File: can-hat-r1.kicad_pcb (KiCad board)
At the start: 2 copper layers, 65 x 55 mm, 61 parts, among them P1 PINBALL-CONNECTOR, P2 PINBALL-CONNECTOR, P3 PIHAT, Q1 DMG2305UX, Q2 DMMT5401, U1 MCP2562, U2 MCP2515, U3 AP3513E, U4 CAT24C32, X1 CRYSTAL

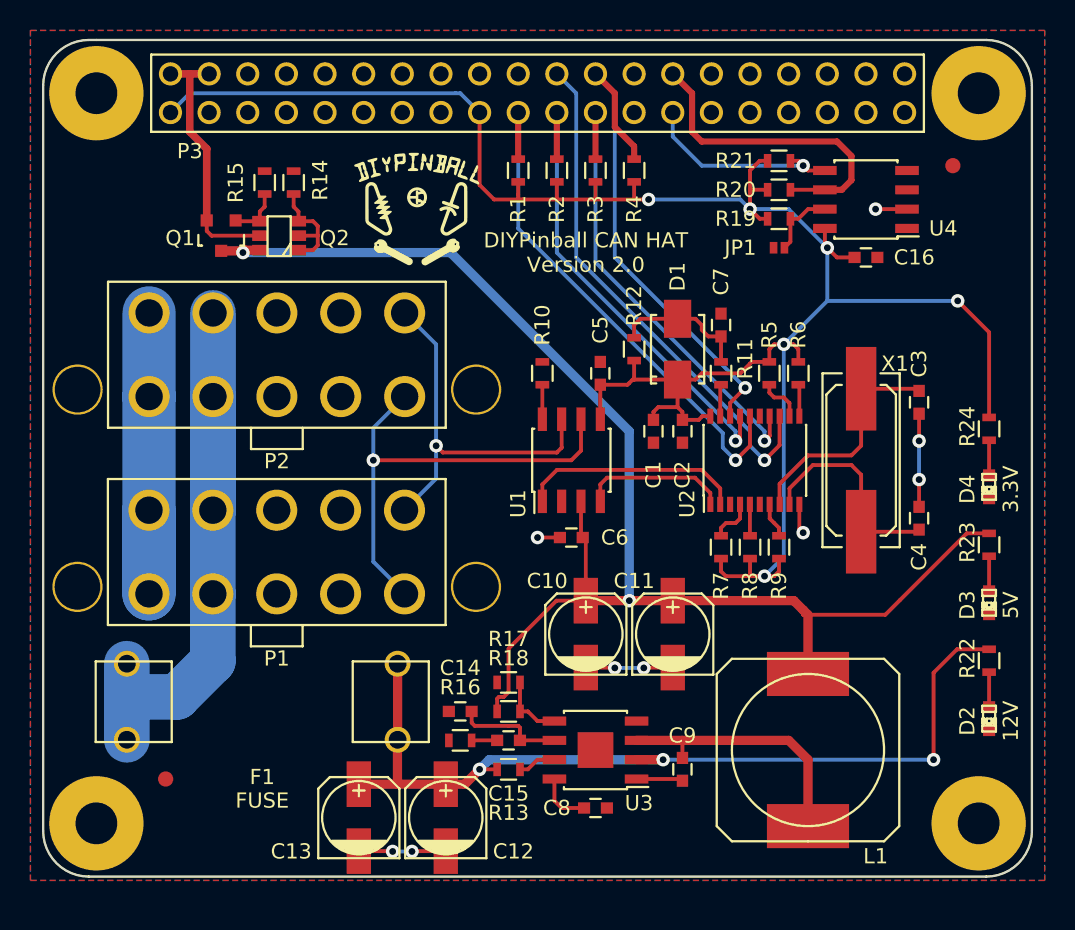
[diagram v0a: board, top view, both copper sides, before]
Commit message: Updating to correct wrong board dimensions (was 1mm too short) and to fix copper around screw holes (there shouldn't be any).
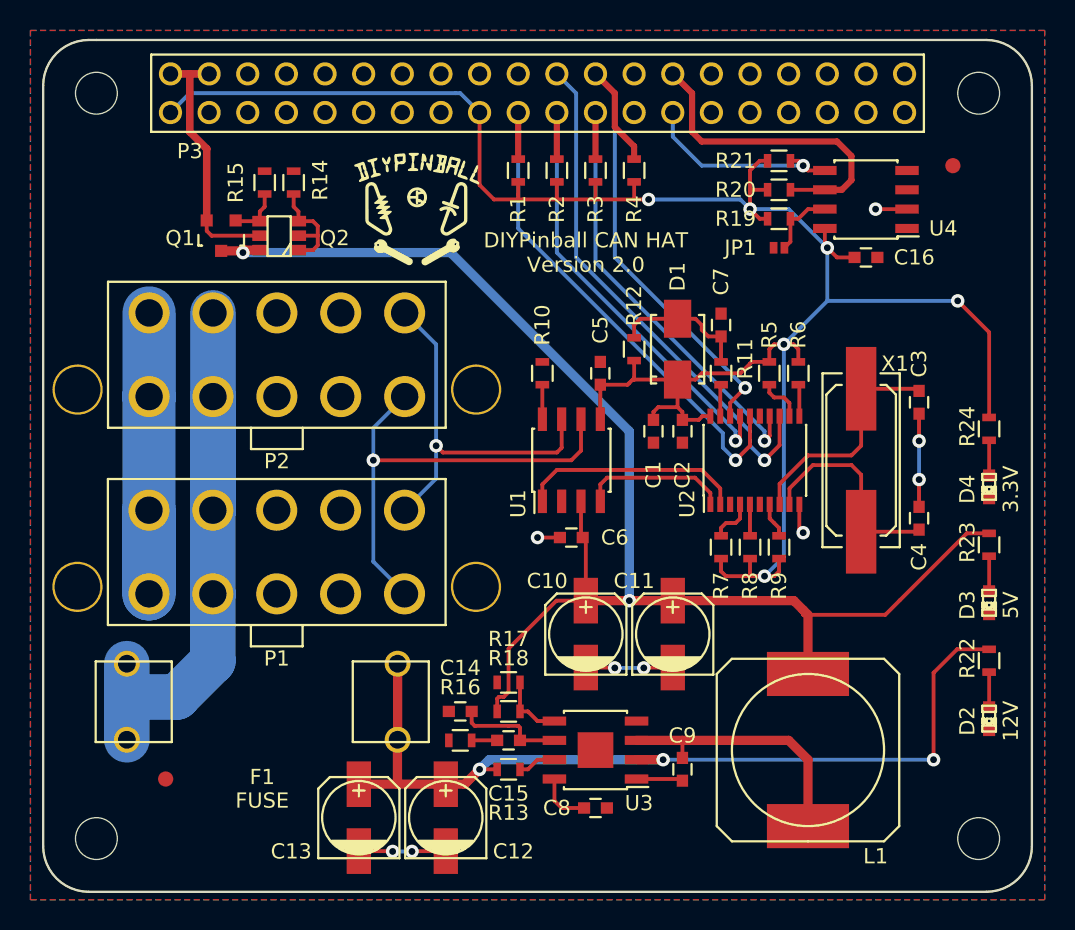
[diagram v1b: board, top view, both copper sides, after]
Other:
- board size 65 x 55 mm -> 65 x 56 mm

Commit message: Updated to latest version of KiCAD. Added PDF of schematic.
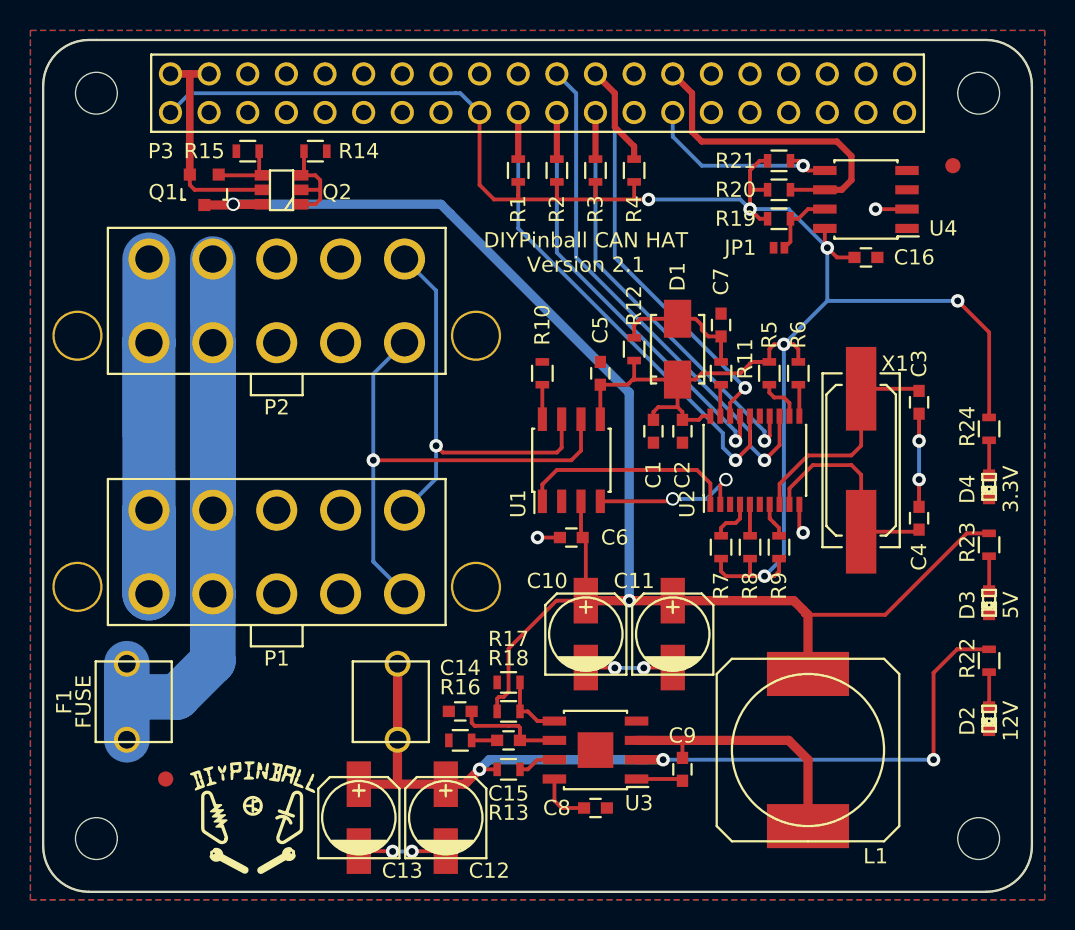
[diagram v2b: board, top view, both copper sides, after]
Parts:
- moved G*** 41.4 mm to (192.7, 150.2)
- moved P2 3.54 mm to (194.3, 116.2)
- moved Q1 3.21 mm to (189.5, 108.9)
- moved Q2 3.02 mm to (194.6, 108.9)
- moved R14 2.51 mm to (196.8, 106.4), turned to 0 degrees
- moved R15 2.34 mm to (192.4, 106.4), turned to 180 degrees
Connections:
- U2 pad 1: Net-(U1-Pad4) -> Net-(U1-Pad1)
- U2 pad 2: Net-(U1-Pad1) -> Net-(U1-Pad4)
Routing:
- net Net-(F1-Pad1): track 42.6 -> 49.7 mm
- net +5V: track 95.4 -> 100.0 mm
- net Net-(P1-Pad5): track 25.1 -> 28.7 mm
- net Net-(P1-Pad1): track 24.0 -> 27.5 mm
- net Net-(P1-Pad10): track 30.7 -> 34.2 mm
- net Net-(P3-Pad2): track 16.9 -> 14.7 mm
- net Net-(Q1-Pad1): track 3.53 -> 4.55 mm
- net Net-(U1-Pad4): track 9.70 -> 10.6 mm, vias 0 -> 2
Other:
- board text added: "DIYPinball CAN HAT Version 2.1"
- board text removed: "DIYPinball CAN HAT Version 2.0"
